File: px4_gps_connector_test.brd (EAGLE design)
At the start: 23.8 x 10.9 mm, 2 parts

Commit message: move via
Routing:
- net GPS_TX: track 18.2 -> 20.2 mm
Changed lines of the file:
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@@
 <contactref element="J1" pad="2"/>
 <contactref element="JP1" pad="1"/>
-<wire x1="16.4592" y1="8.0772" x2="16.4592" y2="7.9248" width="0.1524" layer="1"/>
-<wire x1="15.3162" y1="9.2202" x2="16.4592" y2="8.0772" width="0.1524" layer="1"/>
-<wire x1="7.7724" y1="9.2202" x2="15.3162" y2="9.2202" width="0.1524" layer="16"/>
-<wire x1="3.5814" y1="5.0292" x2="7.7724" y2="9.2202" width="0.1524" layer="16"/>
+<wire x1="16.5862" y1="9.9822" x2="16.4592" y2="9.8552" width="0.1524" layer="1"/>
+<wire x1="16.4592" y1="9.8552" x2="16.4592" y2="7.9248" width="0.1524" layer="1"/>
+<wire x1="8.5344" y1="9.9822" x2="16.5862" y2="9.9822" width="0.1524" layer="16"/>
+<wire x1="3.5814" y1="5.0292" x2="8.5344" y2="9.9822" width="0.1524" layer="16"/>
 <wire x1="3.5814" y1="3.5814" x2="3.5814" y2="5.0292" width="0.1524" layer="16"/>
 <wire x1="2.54" y1="2.54" x2="3.5814" y2="3.5814" width="0.1524" layer="16"/>
 <wire x1="16.4592" y1="7.9248" x2="16.498" y2="7.874" width="0.1524" layer="1"/>
-<via x="15.3162" y="9.2202" extent="1-16" drill="0.35"/>
+<via x="16.5862" y="9.9822" extent="1-16" drill="0.35"/>
 </signal>
 <signal name="GPS_RX">

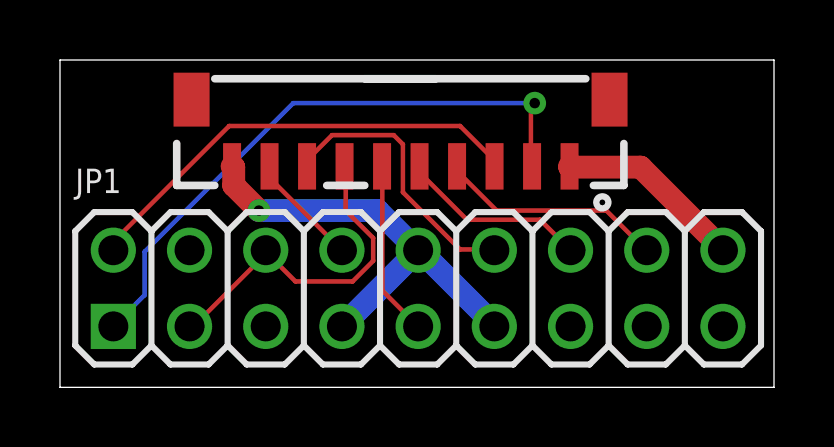
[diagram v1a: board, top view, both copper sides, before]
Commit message: move other via
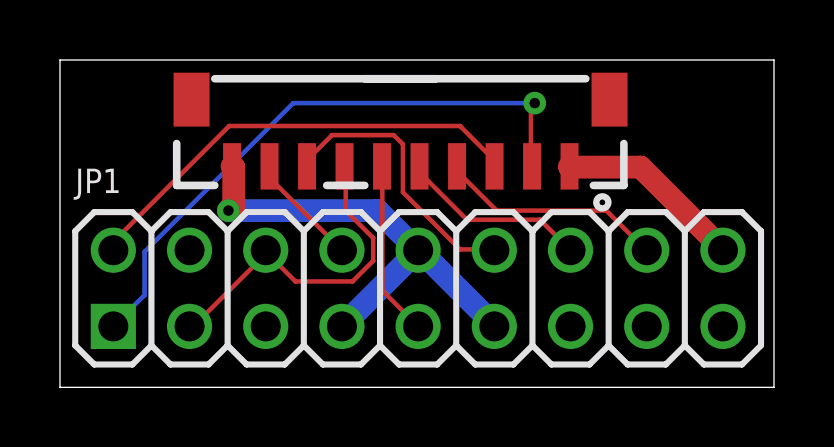
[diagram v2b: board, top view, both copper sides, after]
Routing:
- net GND: track 14.9 -> 15.7 mm
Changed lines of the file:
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@@
 <contactref element="JP1" pad="11"/>
 <contactref element="J1" pad="10"/>
-<wire x1="6.5532" y1="7.239" x2="6.5532" y2="7.8486" width="0.762" layer="1"/>
-<wire x1="7.3914" y1="6.4008" x2="6.5532" y2="7.239" width="0.762" layer="1"/>
-<wire x1="11.3538" y1="6.4008" x2="7.3914" y2="6.4008" width="0.762" layer="16"/>
+<wire x1="6.3754" y1="6.4008" x2="6.5532" y2="6.5786" width="0.762" layer="1"/>
+<wire x1="6.5532" y1="7.8486" x2="6.5532" y2="6.5786" width="0.762" layer="1"/>
+<wire x1="11.3538" y1="6.4008" x2="6.3754" y2="6.4008" width="0.762" layer="16"/>
 <wire x1="12.6492" y1="5.1054" x2="11.3538" y2="6.4008" width="0.762" layer="16"/>
 <wire x1="6.5532" y1="7.8486" x2="6.498" y2="7.874" width="0.762" layer="1"/>
@@
 <wire x1="15.24" y1="2.5908" x2="15.24" y2="2.54" width="0.762" layer="16"/>
 <wire x1="12.954" y1="4.8768" x2="12.7" y2="5.08" width="0.762" layer="16"/>
-<via x="7.3914" y="6.4008" extent="1-16" drill="0.35"/>
+<via x="6.3754" y="6.4008" extent="1-16" drill="0.35"/>
 </signal>
 <signal name="VCC" class="3">
